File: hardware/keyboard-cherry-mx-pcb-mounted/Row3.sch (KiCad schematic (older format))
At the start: 28 parts, among them SW60 Caps lock, SW61 k, SW62 a, SW63 l, SW64 s, SW65 ;, SW66 d, SW67 ', SW68 f, SW69 Enter, SW70 g, SW71 PgDn, SW72 h, SW73 j

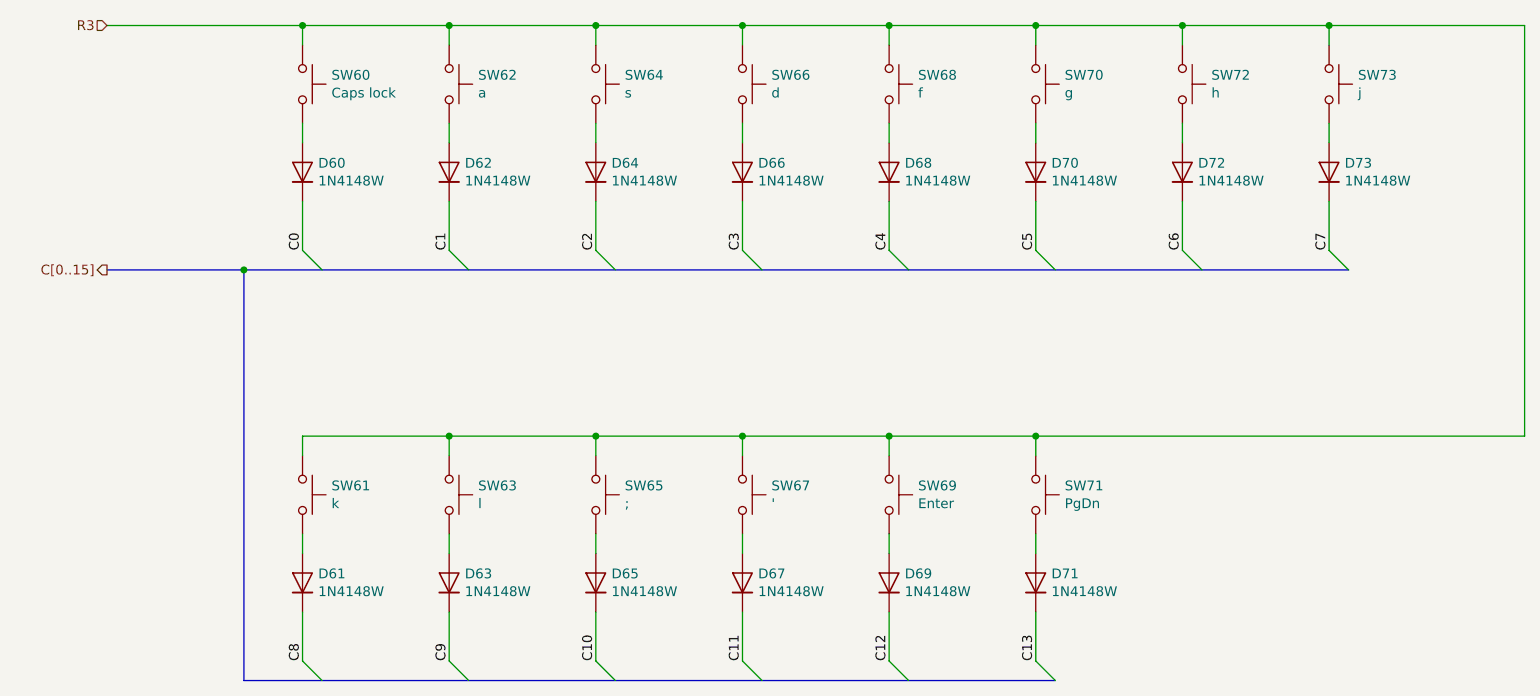
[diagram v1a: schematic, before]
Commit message: Adds completed sensor and power connections. Still need to add USB footprint then sch are done for version 1.0
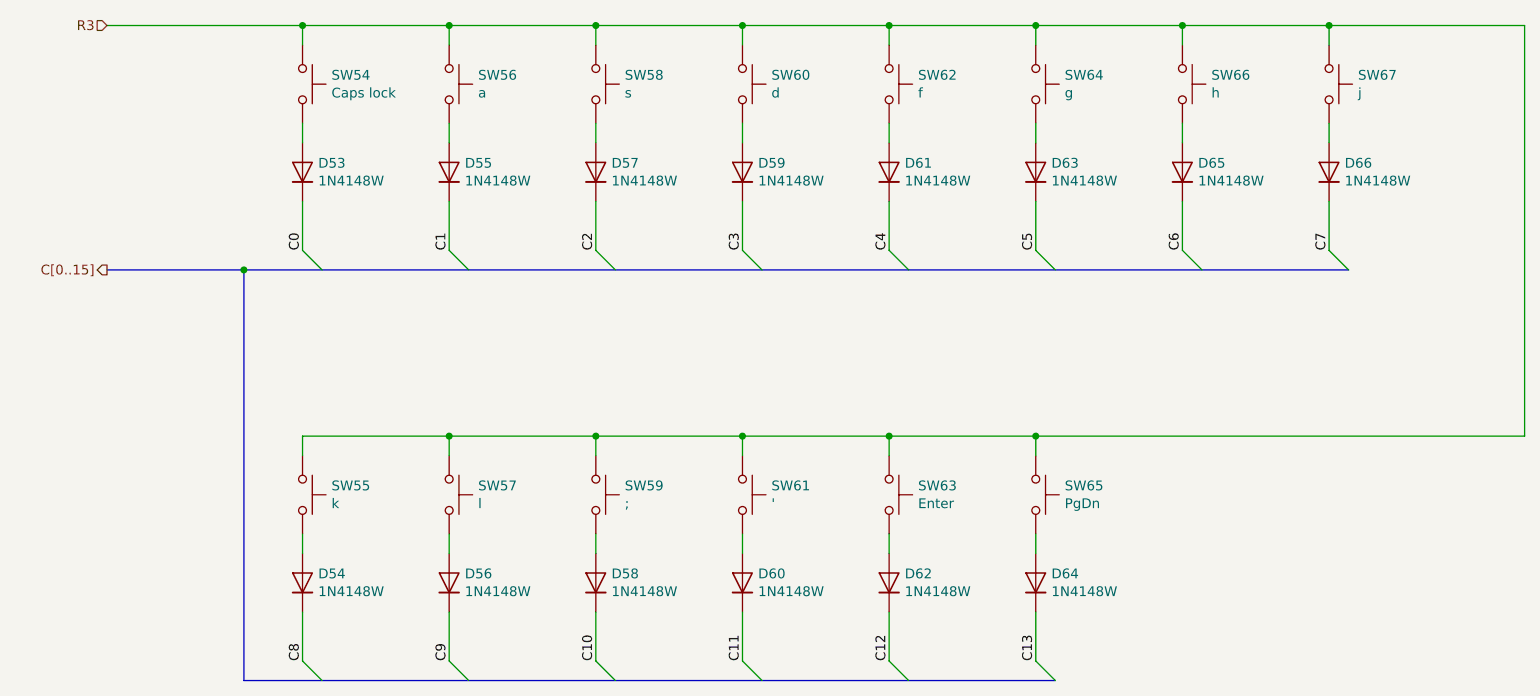
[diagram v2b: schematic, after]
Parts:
- renumbered D60 to D53, D61 to D54, D62 to D55, D63 to D56, D64 to D57, D65 to D58, D66 to D59, D67 to D60, D68 to D61, D69 to D62, D70 to D63, D71 to D64, D72 to D65, D73 to D66, SW60 to SW54, SW61 to SW55, SW62 to SW56, SW63 to SW57, SW64 to SW58, SW65 to SW59, SW66 to SW60, SW67 to SW61, SW68 to SW62, SW69 to SW63, SW70 to SW64, SW71 to SW65, SW72 to SW66, SW73 to SW67

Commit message: Aligns the keys so the column connections are more consistent. e.g. right most keys will have same column connection.
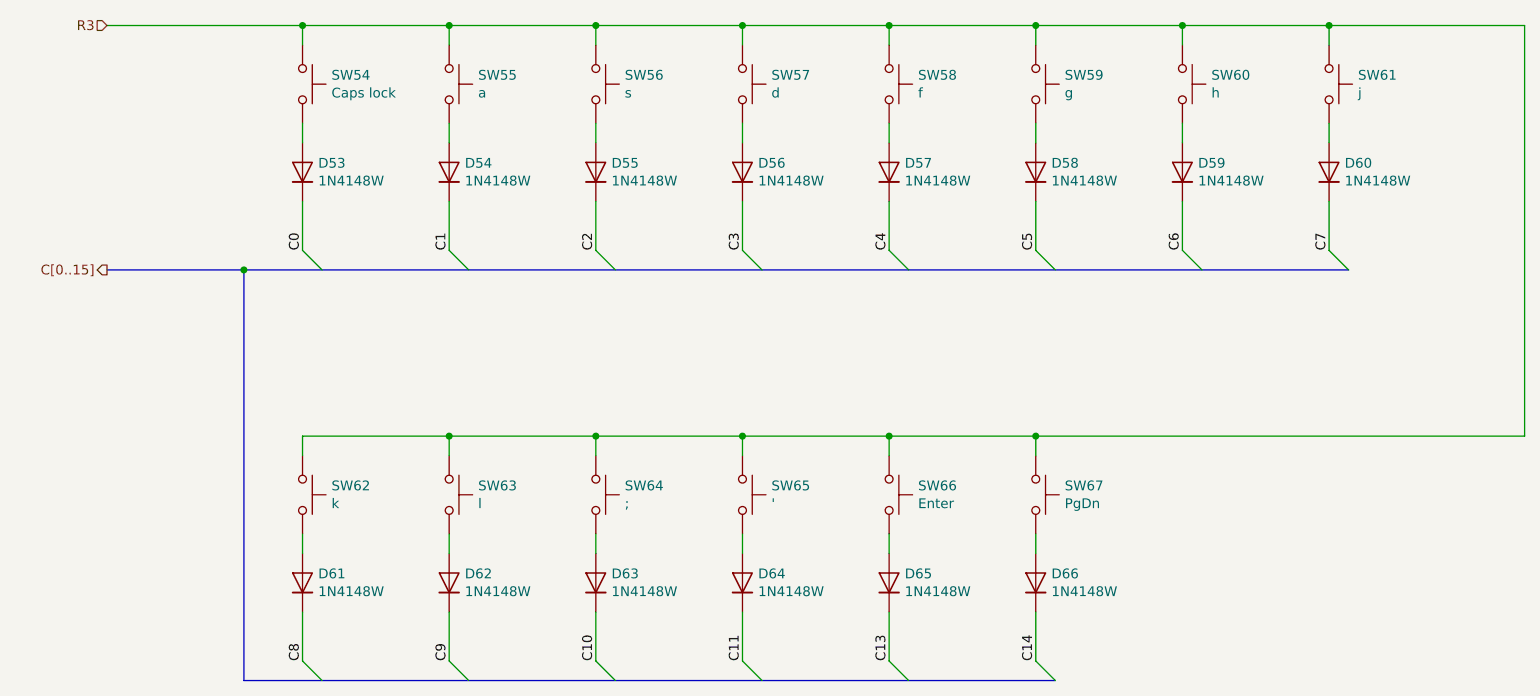
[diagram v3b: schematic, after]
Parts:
- renumbered D55 to D54, D57 to D55, D59 to D56, D61 to D57, D63 to D58, D65 to D59, D66 to D60, D54 to D61, D56 to D62, D58 to D63, D60 to D64, D62 to D65, D64 to D66, SW56 to SW55, SW58 to SW56, SW60 to SW57, SW62 to SW58, SW64 to SW59, SW66 to SW60, SW67 to SW61, SW55 to SW62, SW57 to SW63, SW59 to SW64, SW61 to SW65, SW63 to SW66, SW65 to SW67
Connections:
- net C12 is gone; now on net C13: D65.1 (K)
- net C13: no longer D66.1 (K)
- new net C14: D66.1 (K)

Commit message: Adds labels for each key and creates gerber files.
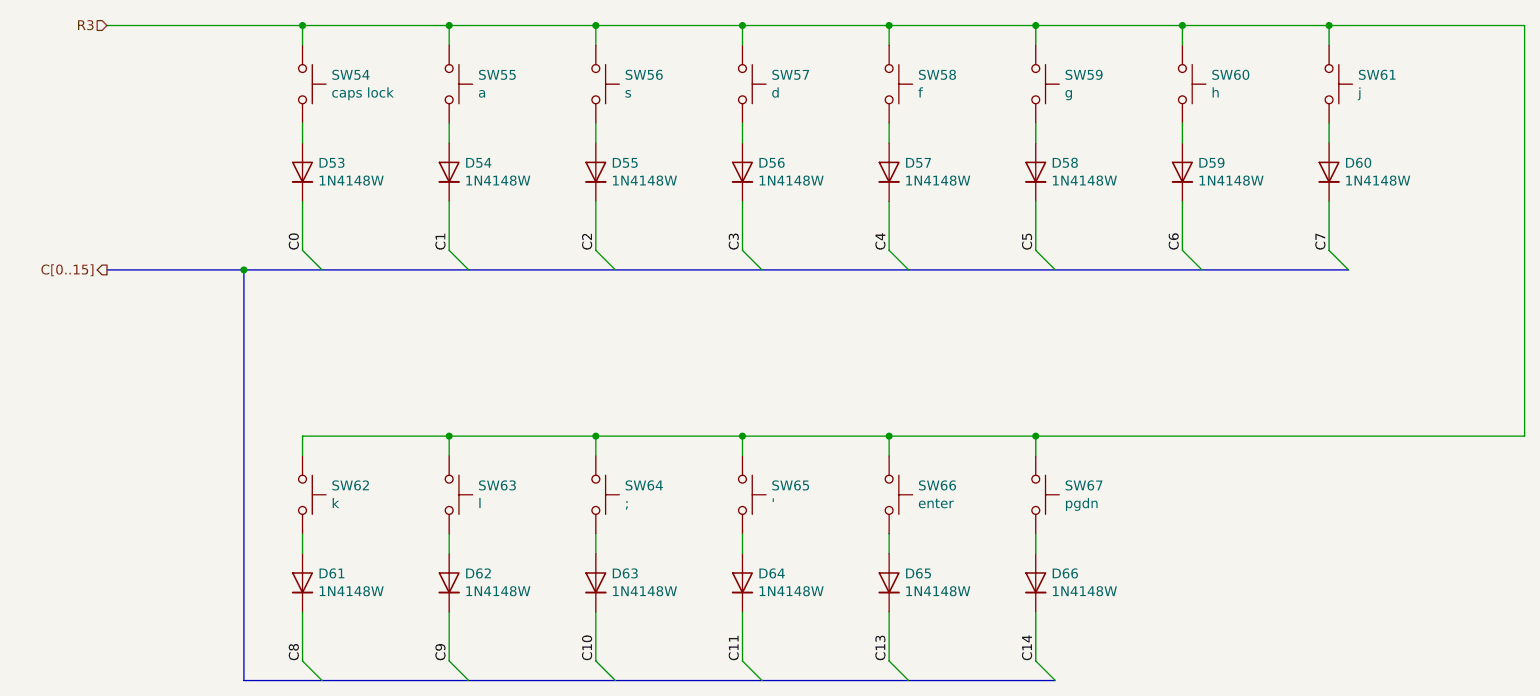
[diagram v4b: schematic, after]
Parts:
- SW54: value Caps lock -> caps lock
- SW66: value Enter -> enter
- SW67: value PgDn -> pgdn
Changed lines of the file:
@@
 AR Path="/5E697948/5E78C3AE/5E78CA63" Ref="SW?"  Part="1"
 F 0 "SW54" V 3104 2548 50  0000 L CNN
-F 1 "Caps lock" V 3195 2548 50  0000 L CNN
+F 1 "caps lock" V 3195 2548 50  0000 L CNN
 F 2 "Button_Switch_Keyboard:SW_Cherry_MX_1.75u_PCB" H 3150 2600 50  0001 C CNN
 F 3 "~" H 3150 2600 50  0001 C CNN
@@
 AR Path="/5E697948/5E78C3AE/5E78CA7B" Ref="SW?"  Part="1"
 F 0 "SW66" V 6104 4648 50  0000 L CNN
-F 1 "Enter" V 6195 4648 50  0000 L CNN
+F 1 "enter" V 6195 4648 50  0000 L CNN
 F 2 "Button_Switch_Keyboard:SW_Cherry_MX_2.25u_PCB" H 6150 4700 50  0001 C CNN
 F 3 "~" H 6150 4700 50  0001 C CNN
@@
 AR Path="/5E697948/5E78C3AE/5E78CA7D" Ref="SW?"  Part="1"
 F 0 "SW67" V 6854 4648 50  0000 L CNN
-F 1 "PgDn" V 6945 4648 50  0000 L CNN
+F 1 "pgdn" V 6945 4648 50  0000 L CNN
 F 2 "Button_Switch_Keyboard:SW_Cherry_MX_1.00u_PCB" H 6900 4700 50  0001 C CNN
 F 3 "~" H 6900 4700 50  0001 C CNN
